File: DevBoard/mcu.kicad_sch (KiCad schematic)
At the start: 47 parts, among them J301 SWD, J302 UART debug, J303 Spare GPIO, SW301 RESET, U301 CC2340R5MODA, U302 TMP1075, U303 TMP1075, U304 TMP1075, U305 TMP1075, U306 TMP1075

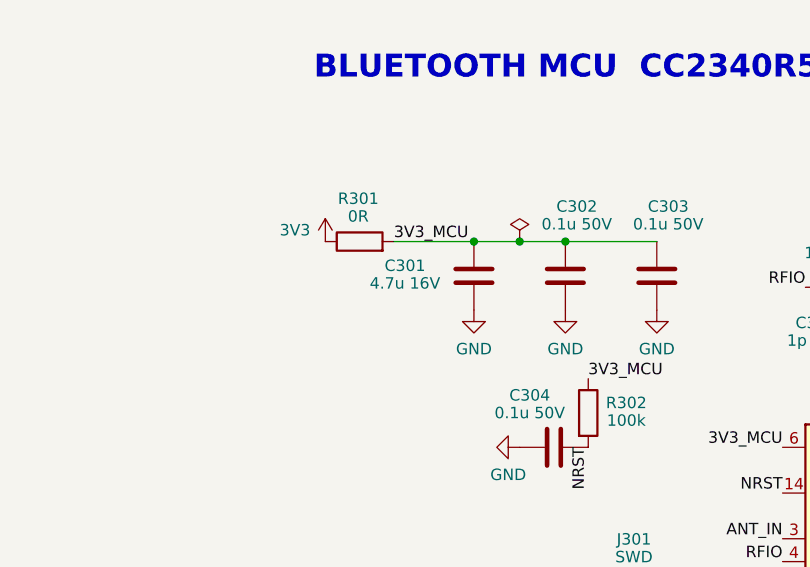
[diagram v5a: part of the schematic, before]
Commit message: Dev board: downsize passives to 0402 where basic parts allow
160 resistors and capacitors move to the smallest package that keeps their
rating: never below 0402, and no JLC basic part becomes extended. Connectivity
and ERC are unchanged, extended parts stay at 27, and the cost goes from
$108.49 to $107.93 per board at 2 boards. Applied by
tools/downsize_passives.py (one-shot); README item 45 lists what moved, what
stayed and why. The PCB still needs Update PCB from Schematic.

Co-Authored-By: Claude Opus 5.5 <noreply@anthropic.com>
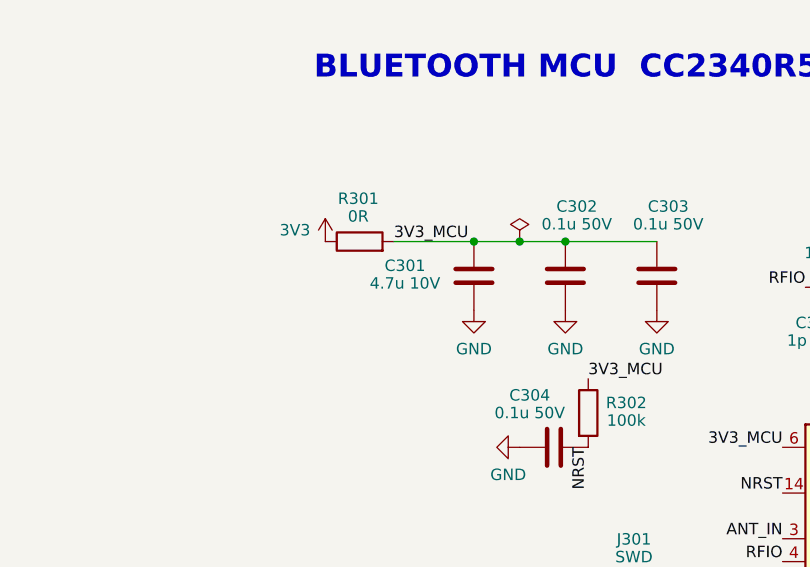
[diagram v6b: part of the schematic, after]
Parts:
- C301: value 4.7u 16V -> 4.7u 10V; footprint Capacitor_SMD:C_0603_1608Metric -> Capacitor_SMD:C_0402_1005Metric; LCSC C19666 -> C23733; MPN CL10A475KO8NNNC -> CL05A475MP5NRNC
- R302, R315: footprint Resistor_SMD:R_0603_1608Metric -> Resistor_SMD:R_0402_1005Metric; LCSC C25803 -> C25741; MPN 0603WAF1003T5E -> 0402WGF1003TCE
- R304, R305: footprint Resistor_SMD:R_0603_1608Metric -> Resistor_SMD:R_0402_1005Metric; LCSC C22978 -> C25890; MPN 0603WAF3301T5E -> 0402WGF3301TCE
- R306: footprint Resistor_SMD:R_0603_1608Metric -> Resistor_SMD:R_0402_1005Metric; LCSC C23138 -> C25104; MPN 0603WAF3300T5E -> 0402WGF3300TCE
- R307, R312: footprint Resistor_SMD:R_0603_1608Metric -> Resistor_SMD:R_0402_1005Metric; LCSC C21189 -> C17168; MPN 0603WAF0000T5E -> 0402WGF0000TCE
- R314: footprint Resistor_SMD:R_0603_1608Metric -> Resistor_SMD:R_0402_1005Metric; LCSC C25819 -> C25792; MPN 0603WAF4702T5E -> 0402WGF4702TCE
- R317, R318, R319, R322, R323, R324: footprint Resistor_SMD:R_0603_1608Metric -> Resistor_SMD:R_0402_1005Metric; LCSC C21190 -> C11702; MPN 0603WAF1001T5E -> 0402WGF1001TCE
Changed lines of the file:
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@@
 			)
 		)
-		(property "Footprint" "Resistor_SMD:R_0603_1608Metric"
+		(property "Footprint" "Resistor_SMD:R_0402_1005Metric"
 			(at 264.16 190.5 0)
 			(hide yes)
@@
 			)
 		)
-		(property "LCSC" "C25819"
+		(property "LCSC" "C25792"
 			(at 264.16 190.5 0)
 			(hide yes)
@@
 			)
 		)
-		(property "MPN" "0603WAF4702T5E"
+		(property "MPN" "0402WGF4702TCE"
 			(at 264.16 190.5 0)
 			(hide yes)
@@
 			)
 		)
-		(property "Footprint" "Resistor_SMD:R_0603_1608Metric"
+		(property "Footprint" "Resistor_SMD:R_0402_1005Metric"
 			(at 55.88 245.618 90)
 			(hide yes)
@@
 			)
 		)
-		(property "LCSC" "C23138"
+		(property "LCSC" "C25104"
 			(at 55.88 243.84 0)
 			(hide yes)
@@
 			)
 		)
-		(property "MPN" "0603WAF3300T5E"
+		(property "MPN" "0402WGF3300TCE"
 			(at 55.88 243.84 0)
 			(hide yes)
@@
 			)
 		)
-		(property "Footprint" "Resistor_SMD:R_0603_1608Metric"
+		(property "Footprint" "Resistor_SMD:R_0402_1005Metric"
 			(at 276.86 190.5 0)
 			(hide yes)
@@
 			)
 		)
-		(property "LCSC" "C25803"
+		(property "LCSC" "C25741"
 			(at 276.86 190.5 0)
 			(hide yes)
@@
 			)
 		)
-		(property "MPN" "0603WAF1003T5E"
+		(property "MPN" "0402WGF1003TCE"
 			(at 276.86 190.5 0)
 			(hide yes)
@@
 			)
 		)
-		(property "Value" "4.7u 16V"
+		(property "Value" "4.7u 10V"
 			(at 132.04 106.24 0)
 			(show_name no)
@@
 			)
 		)
-		(property "Footprint" "Capacitor_SMD:C_0603_1608Metric"
+		(property "Footprint" "Capacitor_SMD:C_0402_1005Metric"
 			(at 140.665 101.6 0)
 			(hide yes)
@@
 			)
 		)
-		(property "LCSC" "C19666"
+		(property "LCSC" "C23733"
 			(at 139.7 105.41 0)
 			(hide yes)
@@
 			)
 		)
-		(property "MPN" "CL10A475KO8NNNC"
+		(property "MPN" "CL05A475MP5NRNC"
 			(at 139.7 105.41 0)
 			(hide yes)
@@
 			)
 		)
-		(property "Footprint" "Resistor_SMD:R_0603_1608Metric"
+		(property "Footprint" "Resistor_SMD:R_0402_1005Metric"
 			(at 86.36 245.618 90)
 			(hide yes)
@@
 			)
 		)
-		(property "LCSC" "C21189"
+		(property "LCSC" "C17168"
 			(at 86.36 243.84 0)
 			(hide yes)
@@
 			)
 		)
-		(property "MPN" "0603WAF0000T5E"
+		(property "MPN" "0402WGF0000TCE"
 			(at 86.36 243.84 0)
 			(hide yes)
@@
 			)
 		)
-		(property "Footprint" "Resistor_SMD:R_0603_1608Metric"
+		(property "Footprint" "Resistor_SMD:R_0402_1005Metric"
 			(at 231.902 190.5 90)
 			(hide yes)
@@
 			)
 		)
-		(property "LCSC" "C22978"
+		(property "LCSC" "C25890"
 			(at 233.68 190.5 0)
 			(hide yes)
@@
 			)
 		)
-		(property "MPN" "0603WAF3301T5E"
+		(property "MPN" "0402WGF3301TCE"
 			(at 233.68 190.5 0)
 			(hide yes)
@@
 			)
 		)
-		(property "Footprint" "Resistor_SMD:R_0603_1608Metric"
+		(property "Footprint" "Resistor_SMD:R_0402_1005Metric"
 			(at 124.46 55.88 0)
 			(hide yes)
@@
 			)
 		)
-		(property "LCSC" "C21190"
+		(property "LCSC" "C11702"
 			(at 124.46 55.88 0)
 			(hide yes)
@@
 			)
 		)
-		(property "MPN" "0603WAF1001T5E"
+		(property "MPN" "0402WGF1001TCE"
 			(at 124.46 55.88 0)
 			(hide yes)
@@
 			)
 		)
-		(property "Footprint" "Resistor_SMD:R_0603_1608Metric"
+		(property "Footprint" "Resistor_SMD:R_0402_1005Metric"
 			(at 218.44 186.69 0)
 			(hide yes)
@@
 			)
 		)
-		(property "LCSC" "C21189"
+		(property "LCSC" "C17168"
 			(at 218.44 186.69 0)
 			(hide yes)
@@
 			)
 		)
-		(property "MPN" "0603WAF0000T5E"
+		(property "MPN" "0402WGF0000TCE"
 			(at 218.44 186.69 0)
 			(hide yes)
@@
 			)
 		)
-		(property "Footprint" "Resistor_SMD:R_0603_1608Metric"
+		(property "Footprint" "Resistor_SMD:R_0402_1005Metric"
 			(at 247.142 190.5 90)
 			(hide yes)
@@
 			)
 		)
-		(property "LCSC" "C22978"
+		(property "LCSC" "C25890"
 			(at 248.92 190.5 0)
 			(hide yes)
@@
 			)
 		)
-		(property "MPN" "0603WAF3301T5E"
+		(property "MPN" "0402WGF3301TCE"
 			(at 248.92 190.5 0)
 			(hide yes)
@@
 			)
 		)
-		(property "Footprint" "Resistor_SMD:R_0603_1608Metric"
+		(property "Footprint" "Resistor_SMD:R_0402_1005Metric"
 			(at 124.46 48.26 0)
 			(hide yes)
@@
 			)
 		)
-		(property "LCSC" "C21190"
+		(property "LCSC" "C11702"
 			(at 124.46 48.26 0)
 			(hide yes)
@@
 			)
 		)
-		(property "MPN" "0603WAF1001T5E"
+		(property "MPN" "0402WGF1001TCE"
 			(at 124.46 48.26 0)
 			(hide yes)
@@
 			)
 		)
-		(property "Footprint" "Resistor_SMD:R_0603_1608Metric"
+		(property "Footprint" "Resistor_SMD:R_0402_1005Metric"
 			(at 124.46 63.5 0)
 			(hide yes)
@@
 			)
 		)
-		(property "LCSC" "C21190"
+		(property "LCSC" "C11702"
 			(at 124.46 63.5 0)
 			(hide yes)
@@
 			)
 		)
-		(property "MPN" "0603WAF1001T5E"
+		(property "MPN" "0402WGF1001TCE"
 			(at 124.46 63.5 0)
 			(hide yes)
@@
 			)
 		)
-		(property "Footprint" "Resistor_SMD:R_0603_1608Metric"
+		(property "Footprint" "Resistor_SMD:R_0402_1005Metric"
 			(at 152.4 120.65 0)
 			(hide yes)
@@
 			)
 		)
-		(property "LCSC" "C25803"
+		(property "LCSC" "C25741"
 			(at 152.4 120.65 0)
 			(hide yes)
@@
 			)
 		)
-		(property "MPN" "0603WAF1003T5E"
+		(property "MPN" "0402WGF1003TCE"
 			(at 152.4 120.65 0)
 			(hide yes)
@@
 			)
 		)
-		(property "Footprint" "Resistor_SMD:R_0603_1608Metric"
+		(property "Footprint" "Resistor_SMD:R_0402_1005Metric"
 			(at 295.91 134.62 0)
 			(hide yes)
@@
 			)
 		)
-		(property "LCSC" "C21190"
+		(property "LCSC" "C11702"
 			(at 295.91 134.62 0)
 			(hide yes)
@@
 			)
 		)
-		(property "MPN" "0603WAF1001T5E"
+		(property "MPN" "0402WGF1001TCE"
 			(at 295.91 134.62 0)
 			(hide yes)
@@
 			)
 		)
-		(property "Footprint" "Resistor_SMD:R_0603_1608Metric"
+		(property "Footprint" "Resistor_SMD:R_0402_1005Metric"
 			(at 295.91 137.16 0)
 			(hide yes)
@@
 			)
 		)
-		(property "LCSC" "C21190"
+		(property "LCSC" "C11702"
 			(at 295.91 137.16 0)
 			(hide yes)
@@
 			)
 		)
-		(property "MPN" "0603WAF1001T5E"
+		(property "MPN" "0402WGF1001TCE"
 			(at 295.91 137.16 0)
 			(hide yes)
@@
 			)
 		)
-		(property "Footprint" "Resistor_SMD:R_0603_1608Metric"
+		(property "Footprint" "Resistor_SMD:R_0402_1005Metric"
 			(at 295.91 160.02 0)
 			(hide yes)
@@
 			)
 		)
-		(property "LCSC" "C21190"
+		(property "LCSC" "C11702"
 			(at 295.91 160.02 0)
 			(hide yes)
@@
 			)
 		)
-		(property "MPN" "0603WAF1001T5E"
+		(property "MPN" "0402WGF1001TCE"
 			(at 295.91 160.02 0)
 			(hide yes)
